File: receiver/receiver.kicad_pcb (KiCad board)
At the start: 2 copper layers, 71.4 x 53.5 mm, 41 parts, among them CON1 AVR-ISP-6, IC1 ATTINY441-SSU, P1 LASER, P2 BATTERY, P3 CONN_01X01, P4 CONN_01X01, Q1 OPTO_NPN, Q2 OPTO_NPN, Q3 OPTO_NPN, Q4 OPTO_NPN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

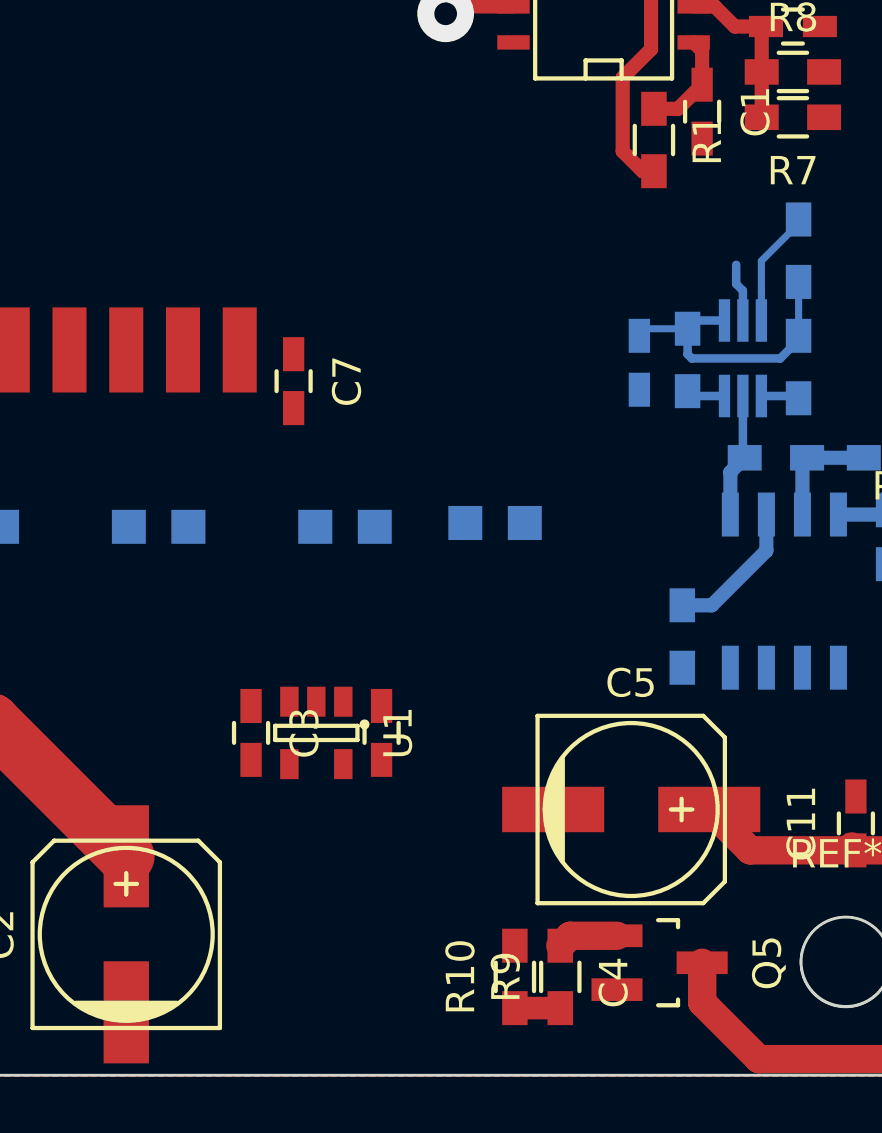
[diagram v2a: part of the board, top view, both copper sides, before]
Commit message: Add a proper symbol for LDO
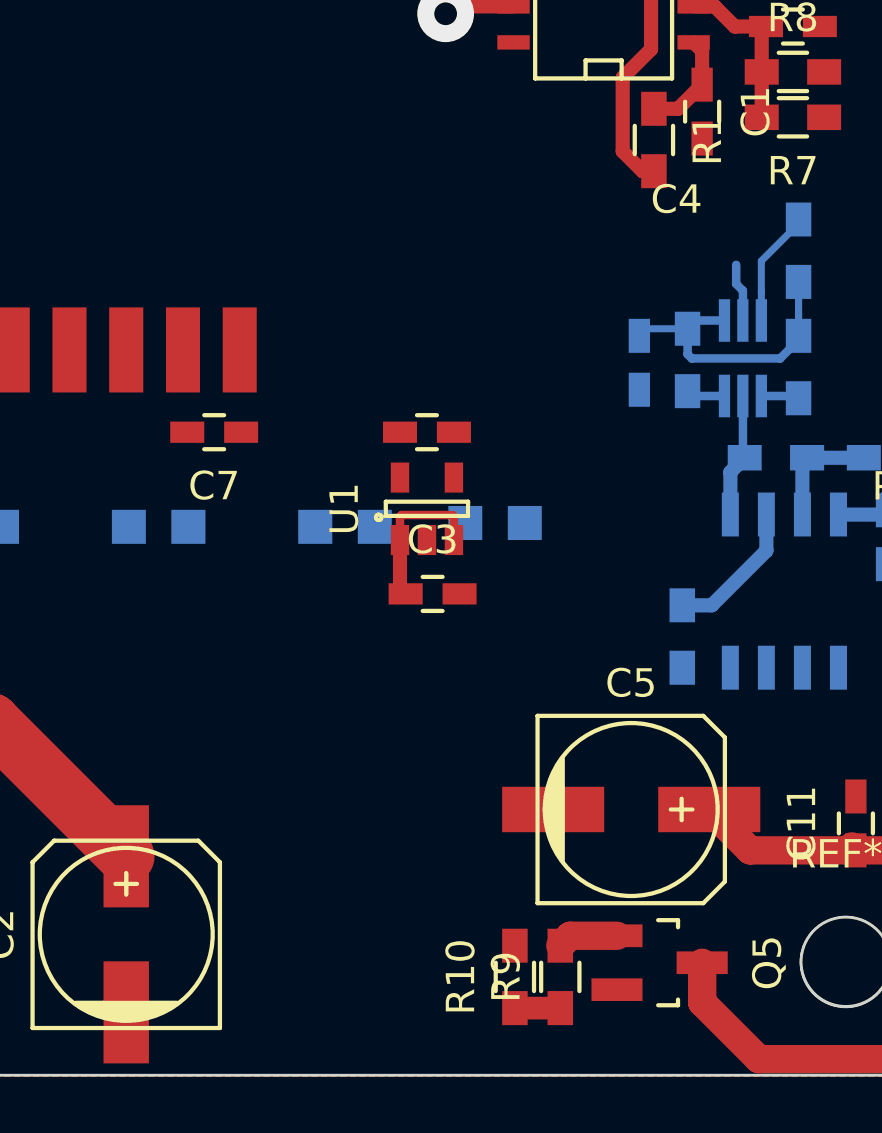
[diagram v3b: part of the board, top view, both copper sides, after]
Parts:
- U1: value MIC5504-3.3 -> MIC5504
- moved C4 10.7 mm to (88.6, 111.3), turned to 0 degrees
- moved U1 8.81 mm to (88.6, 114.0), turned to 90 degrees
- moved C3 8.06 mm to (88.8, 117.0), turned to 0 degrees
- moved C7 3.33 mm to (81.1, 111.3), turned to 180 degrees
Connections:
- U1 pad 1: GND -> VAA
- U1 pad 2: VCC -> GND
- U1 pad 5: (no net) -> VCC
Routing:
- net VAA: track 23.6 -> 29.2 mm
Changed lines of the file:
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@@
 (kicad_pcb (version 4) (host pcbnew 0.201603210401+6634~43~ubuntu14.04.1-product)
   (general
-    (links 89)
-    (no_connects 20)
+    (links 90)
+    (no_connects 18)
     (area 51.452718 80.431499 122.987411 134.017601)
     (thickness 1.6)
     (drawings 425)
-    (tracks 148)
+    (tracks 155)
     (zones 0)
     (modules 41)
@@
   )
   (setup
-    (last_trace_width 0.3)
+    (last_trace_width 0.5)
     (user_trace_width 0.3)
     (user_trace_width 0.5)
@@
   )
   (module Capacitors_SMD:C_0603_HandSoldering (layer F.Cu)
-    (at 82.4 121.9 270)
+    (at 88.8 117)
     (descr "Capacitor SMD 0603, hand soldering")
     (tags "capacitor 0603")
     (attr smd)
-    (fp_text reference C3 (at 0 -1.9 270) (layer F.SilkS)
-      (effects (font (size 1 1) (thickness 0.15)))
-    )
-    (fp_text value C (at 0 1.9 270) (layer F.Fab)
+    (fp_text reference C3 (at 0 -1.9) (layer F.SilkS)
+      (effects (font (size 1 1) (thickness 0.15)))
+    )
+    (fp_text value C (at 0 1.9) (layer F.Fab)
       (effects (font (size 1 1) (thickness 0.15)))
     )
@@
     (fp_line (start -0.35 -0.6) (end 0.35 -0.6) (layer F.SilkS) (width 0.15))
     (fp_line (start 0.35 0.6) (end -0.35 0.6) (layer F.SilkS) (width 0.15))
-    (pad 1 smd rect (at -0.95 0 270) (size 1.2 0.75) (layers F.Cu F.Paste F.Mask)
+    (pad 1 smd rect (at -0.95 0) (size 1.2 0.75) (layers F.Cu F.Paste F.Mask)
       (net 3 VAA))
-    (pad 2 smd rect (at 0.95 0 270) (size 1.2 0.75) (layers F.Cu F.Paste F.Mask)
+    (pad 2 smd rect (at 0.95 0) (size 1.2 0.75) (layers F.Cu F.Paste F.Mask)
       (net 2 GND))
     (model Capacitors_SMD.3dshapes/C_0603_HandSoldering.wrl
@@
   )
   (module Capacitors_SMD:C_0603_HandSoldering (layer F.Cu)
-    (at 87 121.9 270)
+    (at 88.6 111.3)
     (descr "Capacitor SMD 0603, hand soldering")
     (tags "capacitor 0603")
     (attr smd)
-    (fp_text reference C4 (at 8.8 -8.2 270) (layer F.SilkS)
-      (effects (font (size 1 1) (thickness 0.15)))
-    )
-    (fp_text value C (at 0 1.9 270) (layer F.Fab)
+    (fp_text reference C4 (at 8.8 -8.2) (layer F.SilkS)
+      (effects (font (size 1 1) (thickness 0.15)))
+    )
+    (fp_text value C (at 0 1.9) (layer F.Fab)
       (effects (font (size 1 1) (thickness 0.15)))
     )
@@
     (fp_line (start -0.35 -0.6) (end 0.35 -0.6) (layer F.SilkS) (width 0.15))
     (fp_line (start 0.35 0.6) (end -0.35 0.6) (layer F.SilkS) (width 0.15))
-    (pad 1 smd rect (at -0.95 0 270) (size 1.2 0.75) (layers F.Cu F.Paste F.Mask)
+    (pad 1 smd rect (at -0.95 0) (size 1.2 0.75) (layers F.Cu F.Paste F.Mask)
       (net 1 VCC))
-    (pad 2 smd rect (at 0.95 0 270) (size 1.2 0.75) (layers F.Cu F.Paste F.Mask)
+    (pad 2 smd rect (at 0.95 0) (size 1.2 0.75) (layers F.Cu F.Paste F.Mask)
       (net 2 GND))
     (model Capacitors_SMD.3dshapes/C_0603_HandSoldering.wrl
@@
   )
   (module Capacitors_SMD:C_0603_HandSoldering (layer F.Cu)
-    (at 83.9 109.5 270)
+    (at 81.1 111.3 180)
     (descr "Capacitor SMD 0603, hand soldering")
     (tags "capacitor 0603")
     (attr smd)
-    (fp_text reference C7 (at 0 -1.9 270) (layer F.SilkS)
-      (effects (font (size 1 1) (thickness 0.15)))
-    )
-    (fp_text value 1u (at 0 1.9 270) (layer F.Fab)
+    (fp_text reference C7 (at 0 -1.9 180) (layer F.SilkS)
+      (effects (font (size 1 1) (thickness 0.15)))
+    )
+    (fp_text value 1u (at 0 1.9 180) (layer F.Fab)
       (effects (font (size 1 1) (thickness 0.15)))
     )
@@
     (fp_line (start -0.35 -0.6) (end 0.35 -0.6) (layer F.SilkS) (width 0.15))
     (fp_line (start 0.35 0.6) (end -0.35 0.6) (layer F.SilkS) (width 0.15))
-    (pad 1 smd rect (at -0.95 0 270) (size 1.2 0.75) (layers F.Cu F.Paste F.Mask)
+    (pad 1 smd rect (at -0.95 0 180) (size 1.2 0.75) (layers F.Cu F.Paste F.Mask)
       (net 1 VCC))
-    (pad 2 smd rect (at 0.95 0 270) (size 1.2 0.75) (layers F.Cu F.Paste F.Mask)
+    (pad 2 smd rect (at 0.95 0 180) (size 1.2 0.75) (layers F.Cu F.Paste F.Mask)
       (net 2 GND))
     (model Capacitors_SMD.3dshapes/C_0603_HandSoldering.wrl
@@
   )
   (module Housings_SOT-23_SOT-143_TSOT-6:SOT-23-5 (layer F.Cu)
-    (at 84.7 121.9 270)
+    (at 88.6 114 90)
     (descr "5-pin SOT23 package")
     (tags SOT-23-5)
     (attr smd)
-    (fp_text reference U1 (at 0 -2.9 270) (layer F.SilkS)
-      (effects (font (size 1 1) (thickness 0.15)))
-    )
-    (fp_text value MIC5504-3.3 (at 0 2.9 270) (layer F.Fab)
+    (fp_text reference U1 (at 0 -2.9 90) (layer F.SilkS)
+      (effects (font (size 1 1) (thickness 0.15)))
+    )
+    (fp_text value MIC5504 (at 0 2.9 90) (layer F.Fab)
       (effects (font (size 1 1) (thickness 0.15)))
     )
@@
     (fp_line (start -0.25 1.45) (end 0.25 1.45) (layer F.SilkS) (width 0.15))
     (fp_line (start -0.25 -1.45) (end -0.25 1.45) (layer F.SilkS) (width 0.15))
-    (pad 1 smd rect (at -1.1 -0.95 270) (size 1.06 0.65) (layers F.Cu F.Paste F.Mask)
-      (net 2 GND))
-    (pad 2 smd rect (at -1.1 0 270) (size 1.06 0.65) (layers F.Cu F.Paste F.Mask)
+    (pad 1 smd rect (at -1.1 -0.95 90) (size 1.06 0.65) (layers F.Cu F.Paste F.Mask)
+      (net 3 VAA))
+    (pad 2 smd rect (at -1.1 0 90) (size 1.06 0.65) (layers F.Cu F.Paste F.Mask)
+      (net 2 GND))
+    (pad 3 smd rect (at -1.1 0.95 90) (size 1.06 0.65) (layers F.Cu F.Paste F.Mask)
+      (net 3 VAA))
+    (pad 4 smd rect (at 1.1 0.95 90) (size 1.06 0.65) (layers F.Cu F.Paste F.Mask))
+    (pad 5 smd rect (at 1.1 -0.95 90) (size 1.06 0.65) (layers F.Cu F.Paste F.Mask)
       (net 1 VCC))
-    (pad 3 smd rect (at -1.1 0.95 270) (size 1.06 0.65) (layers F.Cu F.Paste F.Mask)
-      (net 3 VAA))
-    (pad 4 smd rect (at 1.1 0.95 270) (size 1.06 0.65) (layers F.Cu F.Paste F.Mask))
-    (pad 5 smd rect (at 1.1 -0.95 270) (size 1.06 0.65) (layers F.Cu F.Paste F.Mask))
     (model Housings_SOT-23_SOT-143_TSOT-6.3dshapes/SOT-23-5.wrl
       (at (xyz 0 0 0))
@@
   (segment (start 99.737321 107.362281) (end 99.737321 106.311711) (width 0.3) (layer B.Cu) (net 2))
   (segment (start 99.737321 106.311711) (end 99.5 106.07439) (width 0.3) (layer B.Cu) (net 2))
+  (segment (start 87.85 117) (end 87.65 116.8) (width 0.5) (layer F.Cu) (net 3))
+  (segment (start 87.65 116.8) (end 87.65 115.1) (width 0.5) (layer F.Cu) (net 3))
+  (segment (start 87.65 115.1) (end 87.65 114.27) (width 0.3) (layer F.Cu) (net 3))
+  (segment (start 87.65 114.27) (end 87.700001 114.219999) (width 0.3) (layer F.Cu) (net 3))
+  (segment (start 87.700001 114.219999) (end 89.499999 114.219999) (width 0.3) (layer F.Cu) (net 3))
+  (segment (start 89.499999 114.219999) (end 89.55 114.27) (width 0.3) (layer F.Cu) (net 3))
+  (segment (start 89.55 114.27) (end 89.55 115.1) (width 0.3) (layer F.Cu) (net 3))
   (segment (start 103.72 126.04) (end 99.99082 126.04) (width 1) (layer F.Cu) (net 3))
   (segment (start 99.99082 126.04) (end 98.55082 124.6) (width 1) (layer F.Cu) (net 3))

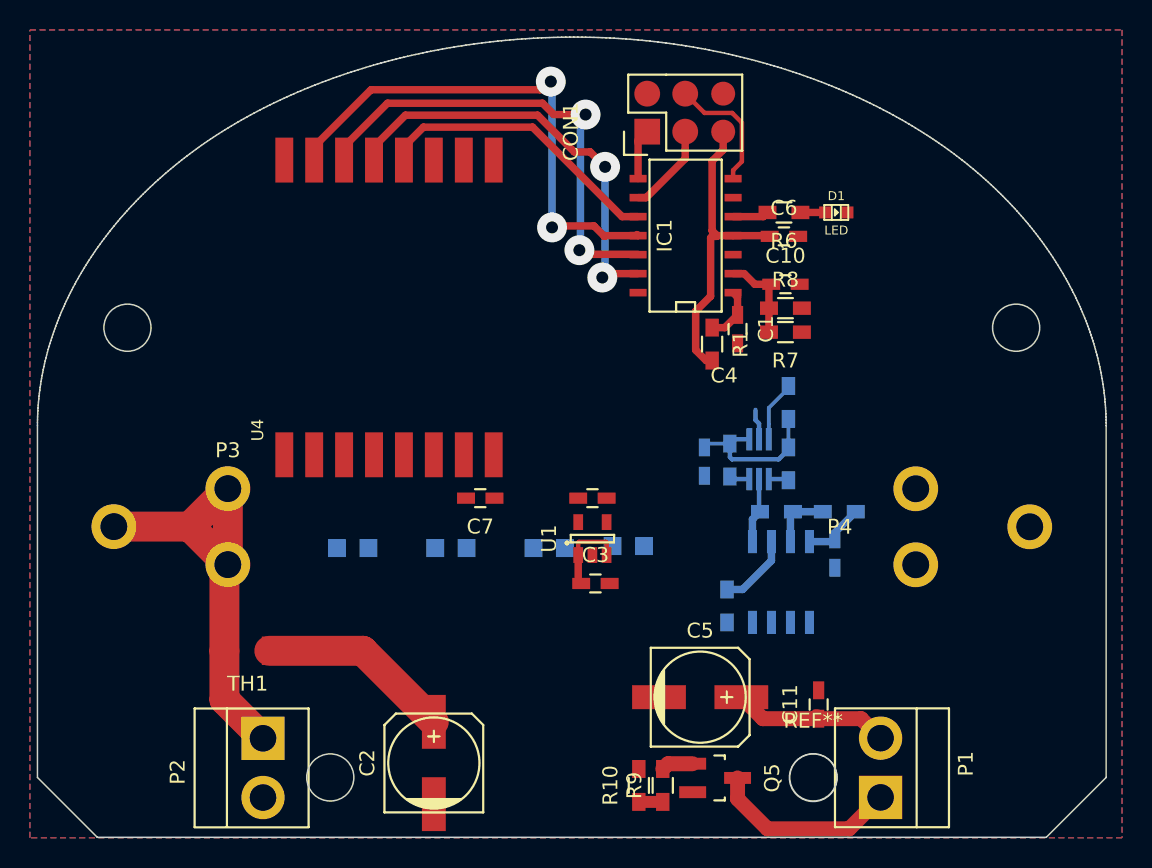
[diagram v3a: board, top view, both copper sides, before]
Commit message: Change digipot to event more expensive but easy to solder SO8 SPI based one
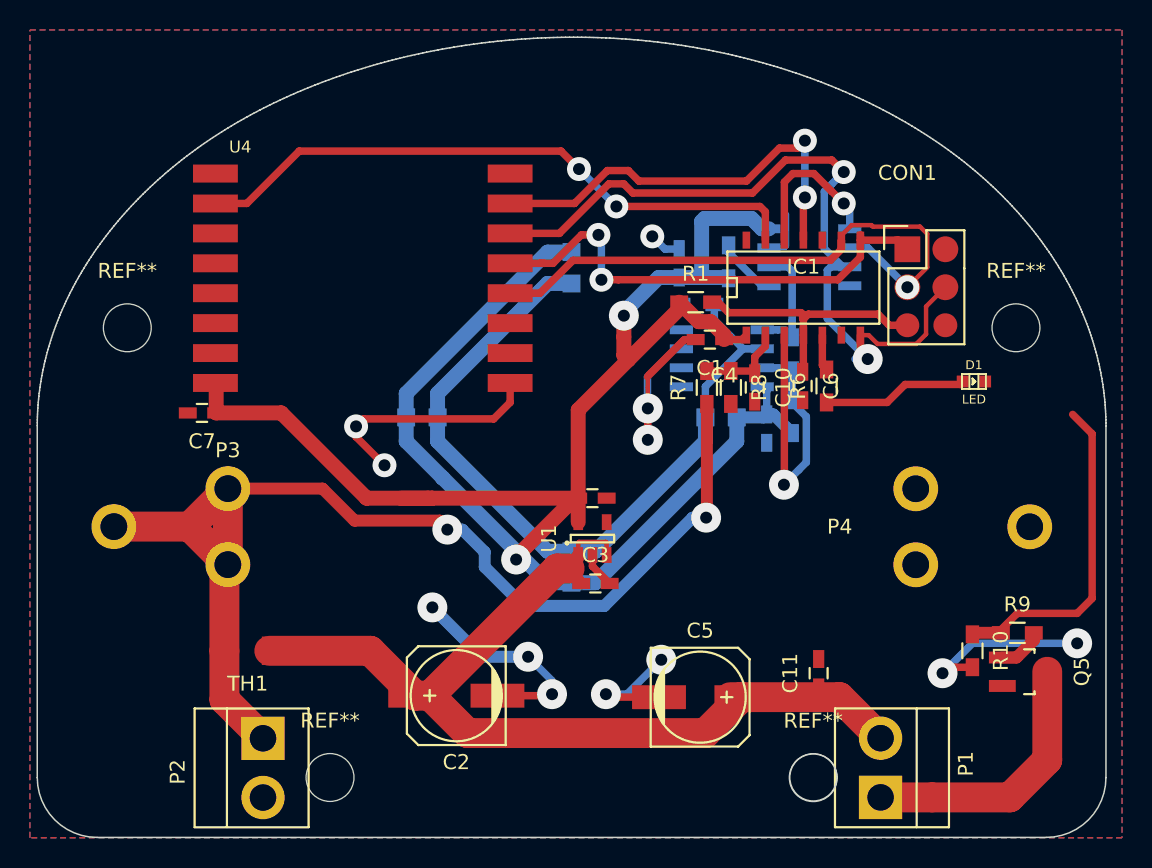
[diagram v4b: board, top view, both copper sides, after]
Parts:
- removed R11, R12: 4.7k, Resistors_SMD:R_0603_HandSoldering
- added REF**: MountingHole_3.2mm_M3_DIN965, Mounting_Holes:MountingHole_3.2mm_M3_DIN965, F.Cu at (116.9, 99.9)
- added REF**: MountingHole_3.2mm_M3_DIN965, Mounting_Holes:MountingHole_3.2mm_M3_DIN965, F.Cu at (57.5, 99.9)
- added REF**: MountingHole_3.2mm_M3_DIN965, Mounting_Holes:MountingHole_3.2mm_M3_DIN965, F.Cu at (71.1, 130.0)
- U3: value MC4018 -> MCP41XXX; footprint Housings_SOT-23_SOT-143_TSOT-6:SC-70-6_Handsoldering -> Housings_SOIC:SOIC-8_3.9x4.9mm_Pitch1.27mm
- moved R9 25.8 mm to (117.0, 120.3), turned to 0 degrees
- moved R10 24.0 mm to (114.0, 121.5), turned to 270 degrees
- moved Q5 21.9 mm to (117.5, 122.9)
- moved R5 20.2 mm to (95.6, 98.3), turned to 180 degrees
- moved C7 19.5 mm to (62.5, 105.6)
- moved CON1 19.1 mm to (109.7, 94.7), turned to 0 degrees
- moved Q2 19.0 mm to (87.2, 95.9), turned to 90 degrees
- moved U4 17.7 mm to (64.8, 89.6), turned to 0 degrees
- moved U2 15.5 mm to (97.2, 102.0), turned to 0 degrees
- moved D1 14.6 mm to (114.1, 103.5)
- moved Q4 14.4 mm to (97.2, 105.9)
- moved U3 13.9 mm to (103.1, 95.2), turned to 180 degrees
- moved C9 13.4 mm to (94.4, 95.6), turned to 90 degrees
- moved R4 13.3 mm to (97.7, 95.5), turned to 90 degrees
- moved R6 11.9 mm to (104.2, 103.8), turned to 90 degrees
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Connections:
- CON1 pad 1: /LASER_ON/MISO -> /MISO
- CON1 pad 3: /SCK/SCL -> /SCK
- CON1 pad 4: /SDA -> /MOSI
- IC1 pad 10: /RADIO_SCK -> (no net)
- IC1 pad 12: /RADIO_MOSI -> /DIGIPOT_SELECT
- IC1 pad 13: /RADIO_MISO -> /INT
- IC1 pad 6: /INT -> /LASER_ON
- IC1 pad 7: /SDA -> /MOSI
- IC1 pad 8: /LASER_ON/MISO -> /MISO
- IC1 pad 9: /SCK/SCL -> /SCK
- R10 pad 1: /LASER_ON/MISO -> /LASER_ON
- R9 pad 1: /LASER_ON/MISO -> /LASER_ON
- U3 pad 1: VCC -> /DIGIPOT_SELECT
- U3 pad 2: GND -> /SCK
- U3 pad 3: /SCK/SCL -> /MOSI
- U3 pad 4: /SDA -> GND
- U3 pad 5: /THRESHOLD -> Net-(R4-Pad2)
- U3 pad 6: Net-(R4-Pad2) -> /THRESHOLD
- U4 pad 12: /RADIO_SCK -> /SCK
- U4 pad 13: /RADIO_MISO -> /MISO
- U4 pad 14: /RADIO_MOSI -> /MOSI
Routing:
- net VCC: track 18.3 -> 136.6 mm, vias 0 -> 2
- net GND: track 2.06 -> 73.4 mm, vias 0 -> 12
- net /MOSI: track 0.00 -> 52.9 mm, vias 0 -> 2
- net /MATRIX_OUT: track 5.04 -> 51.8 mm
- net +BATT: track 30.1 -> 76.0 mm, vias 0 -> 2
- net /INT: track 0.32 -> 41.8 mm, vias 0 -> 2
- net /SCK: track 0.00 -> 40.2 mm, vias 0 -> 1
- net VAA: track 29.2 -> 68.6 mm
- net /MISO: track 0.00 -> 34.9 mm, vias 0 -> 2
- net /RADIO_MOSI: track 31.9 -> 0.00 mm, vias 2 -> 0
- net /RADIO_MISO: track 28.6 -> 0.00 mm, vias 2 -> 0
- net /LASER_ON: track 0.00 -> 22.3 mm
- net /RADIO_SCK: track 19.6 -> 0.00 mm
- net /LASER_DETECT: track 4.07 -> 20.7 mm, vias 0 -> 1
- net /DIGIPOT_SELECT: track 0.00 -> 10.8 mm, vias 0 -> 1
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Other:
- outline, holes or cut-outs redrawn
- net class Default: via_dia 2 -> 1.6
